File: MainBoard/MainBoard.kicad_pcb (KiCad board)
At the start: 2 copper layers, 50 x 50 mm, 12 parts, among them P0n1 ON, P1 CONN_01X07, P13 CONN_01X07, P14 CONN_01X04, P5 BATTERY, P8 CONN_01X04, U1 4056_CARG

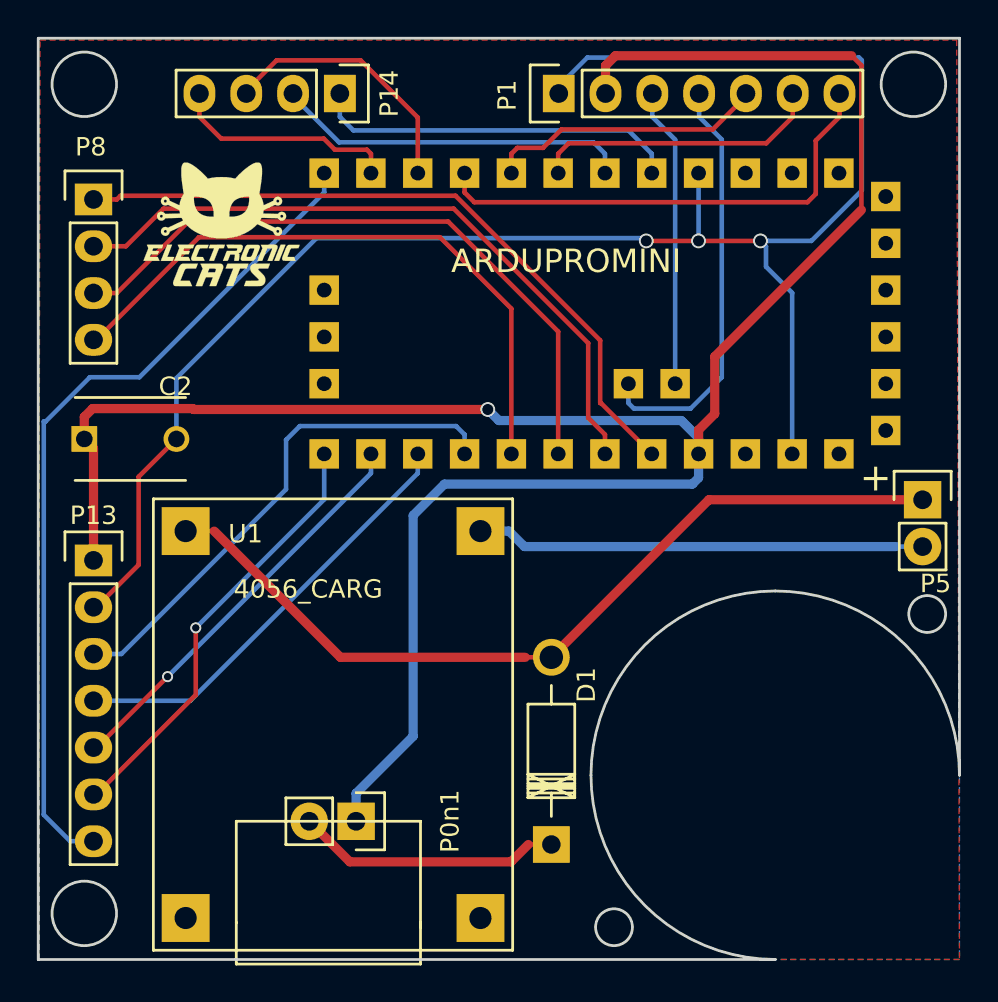
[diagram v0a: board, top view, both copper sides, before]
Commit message: Update referencePCB for schematic MainBoard
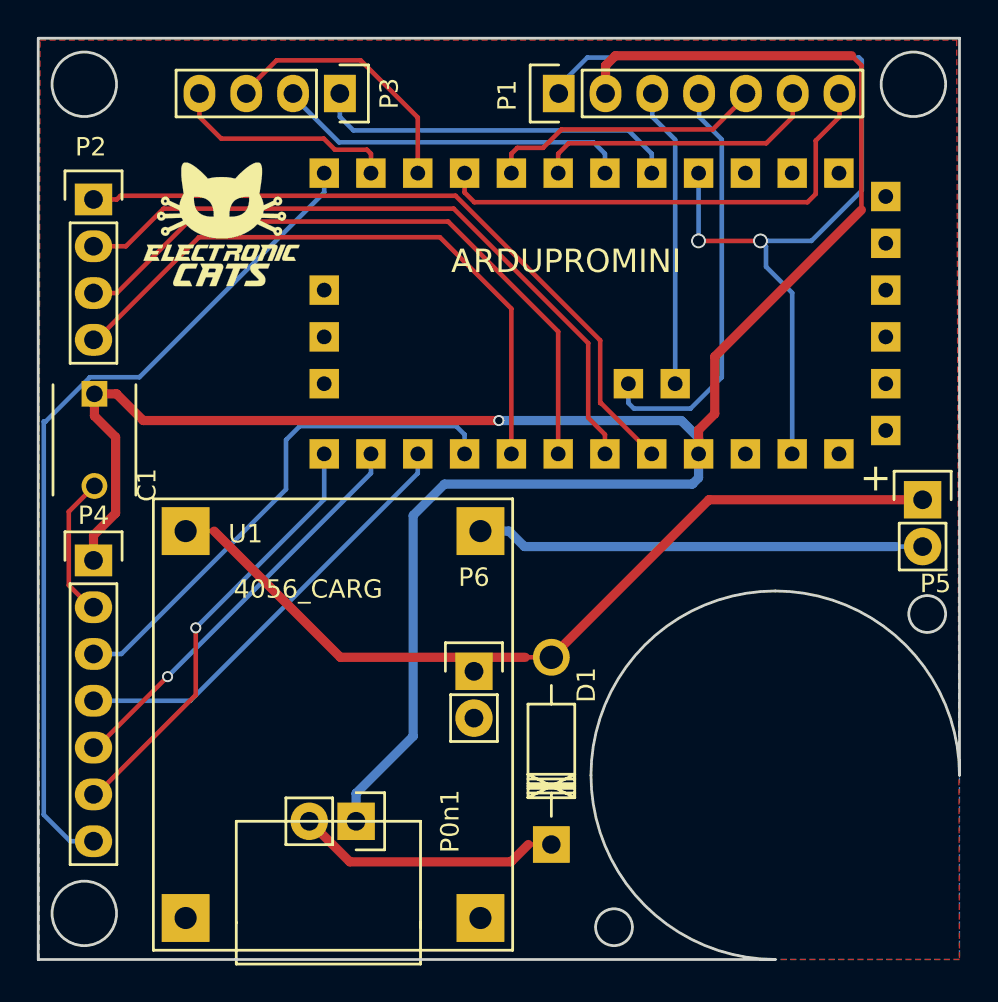
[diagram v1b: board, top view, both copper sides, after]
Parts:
- added P6: BATTERY, Pin_Headers:Pin_Header_Straight_1x02, F.Cu at (108.2, 88.3)
- C1: renamed from C2; value C -> 0.1uF
- P5: value BATTERY -> ON/OFF
- moved C1 2.51 mm to (87.6, 73.2), turned to 270 degrees
- renumbered P8 to P2, P14 to P3, P13 to P4
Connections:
- net A0 renamed /A0
- net A1 renamed /A1
- net A2 renamed /A2
- net A3 renamed /A3
- net D7 renamed /D7
- net D8 renamed /D8
- net DHT/D6 renamed /DHT/D6
- net INT0 renamed /INT0
- net INT1 renamed /INT1
- net MISO renamed /MISO
- net MOSI renamed /MOSI
- net NSS renamed /NSS
- net RST renamed /RST
- net SCK renamed /SCK
- net SCL renamed /SCL
- net SDA renamed /SDA
- net S_RX renamed /S_RX
- net S_TX renamed /S_TX
- P5 pad 1: Net-(D1-Pad2) -> +BATT
- P5 pad 2: Net-(P5-Pad2) -> Net-(D1-Pad1)
- RAW1 pad 1: Net-(RAW1-Pad1) -> (no net)
- RAW1 pad 2: Net-(RAW1-Pad2) -> (no net)
- RAW1 pad 3: Net-(RAW1-Pad3) -> (no net)
- RAW1 pad 4: Net-(RAW1-Pad4) -> (no net)
- RAW1 pad 5: Net-(RAW1-Pad5) -> (no net)
- RAW1 pad 6: Net-(RAW1-Pad6) -> (no net)
- U1 pad 4: Net-(P5-Pad2) -> GND
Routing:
- net Net-(P5-Pad2): track 24.3 -> 0.00 mm
- net GND: track 96.5 -> 81.4 mm, vias 3 -> 2
- net +BATT: track 131.4 -> 144.6 mm
- net Net-(D1-Pad2): track 46.4 -> 34.8 mm
- net Net-(D1-Pad1): track 14.4 -> 15.9 mm

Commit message: Update PCB footprints MainBoard
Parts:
- removed P0n1: ON, Pin_Headers:Pin_Header_Straight_1x02
- moved P5 35.4 mm to (101.8, 96.4), turned to 270 degrees
- moved P6 26.1 mm to (132.6, 79.0)
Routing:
- net GND: track 81.4 -> 93.1 mm
- net +BATT: track 144.6 -> 133.0 mm
- net Net-(D1-Pad2): track 34.8 -> 46.4 mm
- net Net-(D1-Pad1): track 15.9 -> 14.4 mm
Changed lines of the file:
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@@
 (kicad_pcb (version 4) (host pcbnew 4.0.3-stable)
   (general
-    (links 33)
-    (no_connects 3)
+    (links 31)
+    (no_connects 2)
     (area 84.474999 53.824999 134.625001 103.975001)
     (thickness 1.6)
     (drawings 28)
-    (tracks 176)
+    (tracks 183)
     (zones 0)
-    (modules 13)
+    (modules 12)
     (nets 30)
   )
@@
     (add_net /S_RX)
     (add_net /S_TX)
-    (add_net GND)
     (add_net "Net-(D1-Pad1)")
     (add_net "Net-(D1-Pad2)")
@@
     (uvia_drill 0.1)
     (add_net +BATT)
-  )
-  (module Pin_Headers:Pin_Header_Straight_1x02 (layer F.Cu)
-    (at 101.8 96.4 270)
-    (descr "Through hole pin header")
-    (tags "pin header")
-    (fp_text reference P0n1 (at 0 -5.1 270) (layer F.SilkS)
-      (effects (font (size 1 1) (thickness 0.15)))
-    )
-    (fp_text value ON (at 0 -3.1 270) (layer F.Fab)
-      (effects (font (size 1 1) (thickness 0.15)))
-    )
-    (fp_line (start 1.27 1.27) (end 1.27 3.81) (layer F.SilkS) (width 0.15))
-    (fp_line (start 1.55 -1.55) (end 1.55 0) (layer F.SilkS) (width 0.15))
-    (fp_line (start -1.75 -1.75) (end -1.75 4.3) (layer F.CrtYd) (width 0.05))
-    (fp_line (start 1.75 -1.75) (end 1.75 4.3) (layer F.CrtYd) (width 0.05))
-    (fp_line (start -1.75 -1.75) (end 1.75 -1.75) (layer F.CrtYd) (width 0.05))
-    (fp_line (start -1.75 4.3) (end 1.75 4.3) (layer F.CrtYd) (width 0.05))
-    (fp_line (start 1.27 1.27) (end -1.27 1.27) (layer F.SilkS) (width 0.15))
-    (fp_line (start -1.55 0) (end -1.55 -1.55) (layer F.SilkS) (width 0.15))
-    (fp_line (start -1.55 -1.55) (end 1.55 -1.55) (layer F.SilkS) (width 0.15))
-    (fp_line (start -1.27 1.27) (end -1.27 3.81) (layer F.SilkS) (width 0.15))
-    (fp_line (start -1.27 3.81) (end 1.27 3.81) (layer F.SilkS) (width 0.15))
-    (pad 1 thru_hole rect (at 0 0 270) (size 2.032 2.032) (drill 1.016) (layers *.Cu *.Mask F.SilkS)
-      (net 3 +BATT))
-    (pad 2 thru_hole oval (at 0 2.54 270) (size 2.032 2.032) (drill 1.016) (layers *.Cu *.Mask F.SilkS)
-      (net 11 "Net-(D1-Pad1)"))
-    (model Pin_Headers.3dshapes/Pin_Header_Straight_1x02.wrl
-      (at (xyz 0 -0.05 0))
-      (scale (xyz 1 1 1))
-      (rotate (xyz 0 0 90))
-    )
+    (add_net GND)
   )
   (module 4056_lipoCharg (layer F.Cu)
@@
   )
   (module Pin_Headers:Pin_Header_Straight_1x02 (layer F.Cu)
-    (at 132.55 78.95)
+    (at 101.79 96.4 270)
     (descr "Through hole pin header")
     (tags "pin header")
-    (fp_text reference P5 (at 0.7 4.55) (layer F.SilkS)
-      (effects (font (size 1 1) (thickness 0.15)))
-    )
-    (fp_text value ON/OFF (at -1.95 3.05 90) (layer F.Fab)
+    (fp_text reference P5 (at 0.7 4.55 270) (layer F.SilkS)
+      (effects (font (size 1 1) (thickness 0.15)))
+    )
+    (fp_text value ON/OFF (at -1.95 3.05 360) (layer F.Fab)
       (effects (font (size 1 1) (thickness 0.15)))
     )
@@
     (fp_line (start -1.27 1.27) (end -1.27 3.81) (layer F.SilkS) (width 0.15))
     (fp_line (start -1.27 3.81) (end 1.27 3.81) (layer F.SilkS) (width 0.15))
-    (pad 1 thru_hole rect (at 0 0) (size 2.032 2.032) (drill 1.016) (layers *.Cu *.Mask F.SilkS)
+    (pad 1 thru_hole rect (at 0 0 270) (size 2.032 2.032) (drill 1.016) (layers *.Cu *.Mask F.SilkS)
       (net 3 +BATT))
-    (pad 2 thru_hole oval (at 0 2.54) (size 2.032 2.032) (drill 1.016) (layers *.Cu *.Mask F.SilkS)
+    (pad 2 thru_hole oval (at 0 2.54 270) (size 2.032 2.032) (drill 1.016) (layers *.Cu *.Mask F.SilkS)
       (net 11 "Net-(D1-Pad1)"))
     (model Pin_Headers.3dshapes/Pin_Header_Straight_1x02.wrl
@@
   )
   (module Pin_Headers:Pin_Header_Straight_1x02 (layer F.Cu)
-    (at 108.2 88.26)
+    (at 132.575 78.96)
     (descr "Through hole pin header")
     (tags "pin header")
-    (fp_text reference P6 (at 0 -5.1) (layer F.SilkS)
-      (effects (font (size 1 1) (thickness 0.15)))
-    )
-    (fp_text value BATTERY (at 0 -3.1) (layer F.Fab)
+    (fp_text reference P6 (at 0.75 -2.56) (layer F.SilkS)
+      (effects (font (size 1 1) (thickness 0.15)))
+    )
+    (fp_text value BATTERY (at -2.475 2.99 90) (layer F.Fab)
       (effects (font (size 1 1) (thickness 0.15)))
     )
@@
   (gr_line (start 84.55 103.9) (end 84.55 53.9) (layer Edge.Cuts) (width 0.15))
   (gr_line (start 84.55 53.9) (end 134.55 53.9) (layer Edge.Cuts) (width 0.15))
+  (segment (start 120.386543 64.9) (end 123.75 64.9) (width 0.5) (layer F.Cu) (net 1))
+  (segment (start 120.39 61.22) (end 120.39 64.896543) (width 0.5) (layer B.Cu) (net 1))
+  (segment (start 120.39 64.896543) (end 120.386543 64.9) (width 0.5) (layer B.Cu) (net 1))
+  (segment (start 110.94 81.49) (end 128.275 81.49) (width 0.5) (layer B.Cu) (net 1))
+  (segment (start 125.47 77.76) (end 128.275 80.565) (width 0.5) (layer B.Cu) (net 1))
+  (segment (start 128.275 81.49) (end 128.5 81.49) (width 0.5) (layer B.Cu) (net 1))
+  (segment (start 125.47 76.46) (end 125.47 77.76) (width 0.5) (layer B.Cu) (net 1))
+  (segment (start 128.275 80.565) (end 128.275 81.49) (width 0.5) (layer B.Cu) (net 1))
+  (segment (start 125.47 76.46) (end 125.47 67.95) (width 0.5) (layer B.Cu) (net 1))
+  (segment (start 123.75 64.9) (end 123.75 66.23) (width 0.5) (layer B.Cu) (net 1))
+  (segment (start 123.75 66.23) (end 125.47 67.95) (width 0.5) (layer B.Cu) (net 1))
+  (segment (start 131.13816 81.5) (end 131.12816 81.49) (width 0.25) (layer B.Cu) (net 1))
+  (segment (start 128.5 81.49) (end 131.11316 81.49) (width 0.5) (layer B.Cu) (net 1))
+  (segment (start 132.575 81.5) (end 131.13816 81.5) (width 0.25) (layer B.Cu) (net 1))
+  (segment (start 131.12816 81.49) (end 128.5 81.49) (width 0.25) (layer B.Cu) (net 1))
   (segment (start 87.6 78.2) (end 86.208999 79.591001) (width 0.25) (layer F.Cu) (net 1))
   (segment (start 86.208999 79.591001) (end 86.208999 83.591399) (width 0.25) (layer F.Cu) (net 1))
@@
   (segment (start 87.3976 84.78) (end 87.55 84.78) (width 0.25) (layer F.Cu) (net 1))
   (via (at 120.386543 64.9) (size 0.8) (drill 0.6) (layers F.Cu B.Cu) (net 1))
-  (segment (start 120.39 64.896543) (end 120.386543 64.9) (width 0.25) (layer B.Cu) (net 1))
-  (segment (start 120.39 61.22) (end 120.39 64.896543) (width 0.25) (layer B.Cu) (net 1))
-  (segment (start 120.386543 64.9) (end 123.75 64.9) (width 0.25) (layer F.Cu) (net 1))
   (via (at 123.75 64.9) (size 0.8) (drill 0.6) (layers F.Cu B.Cu) (net 1))
-  (segment (start 123.75 64.9) (end 124.049999 65.199999) (width 0.25) (layer B.Cu) (net 1))
   (segment (start 124.174264 64.9) (end 123.75 64.9) (width 0.25) (layer B.Cu) (net 1))
   (segment (start 129.25 55.1) (end 129.25 62.165002) (width 0.25) (layer B.Cu) (net 1))
@@
   (segment (start 126.515002 64.9) (end 124.174264 64.9) (width 0.25) (layer B.Cu) (net 1))
   (segment (start 129.25 62.165002) (end 126.515002 64.9) (width 0.25) (layer B.Cu) (net 1))
-  (segment (start 124.049999 65.199999) (end 124.049999 66.299999) (width 0.25) (layer B.Cu) (net 1))
-  (segment (start 125.47 67.72) (end 125.47 76.46) (width 0.25) (layer B.Cu) (net 1))
-  (segment (start 124.049999 66.299999) (end 125.47 67.72) (width 0.25) (layer B.Cu) (net 1))
   (segment (start 112.8 56.9) (end 112.8 56.5) (width 0.25) (layer B.Cu) (net 1))
   (segment (start 87.55 84.78) (end 87.7024 84.78) (width 0.25) (layer F.Cu) (net 1))
   (segment (start 108.55 80.65) (end 110.1 80.65) (width 0.5) (layer B.Cu) (net 1))
   (segment (start 110.1 80.65) (end 110.94 81.49) (width 0.5) (layer B.Cu) (net 1))
-  (segment (start 110.94 81.49) (end 131.11316 81.49) (width 0.5) (layer B.Cu) (net 1))
+  (segment (start 131.11316 81.49) (end 132.55 81.49) (width 0.25) (layer B.Cu) (net 1))
   (segment (start 92.55 80.65) (end 94.1 80.65) (width 0.25) (layer F.Cu) (net 2))
   (segment (start 94.1 80.65) (end 100.95 87.5) (width 0.5) (layer F.Cu) (net 2))
@@
   (segment (start 100.95 87.5) (end 110.986508 87.5) (width 0.5) (layer F.Cu) (net 2))
   (segment (start 120.95 78.95) (end 112.4 87.5) (width 0.5) (layer F.Cu) (net 2))
+  (segment (start 132.55 78.95) (end 120.95 78.95) (width 0.5) (layer F.Cu) (net 2))
   (segment (start 87.55 82.24) (end 87.55 80.8764) (width 0.5) (layer F.Cu) (net 3))
   (segment (start 87.55 80.8764) (end 88.750001 79.676399) (width 0.5) (layer F.Cu) (net 3))
@@
   (segment (start 90.25 74.65) (end 109.55 74.65) (width 0.5) (layer F.Cu) (net 3))
   (via (at 109.55 74.65) (size 0.6) (drill 0.4) (layers F.Cu B.Cu) (net 3))
-  (segment (start 132.55 78.95) (end 120.95 78.95) (width 0.5) (layer F.Cu) (net 3))
   (segment (start 104.9 79.8) (end 106.6 78.1) (width 0.5) (layer B.Cu) (net 3))
   (segment (start 120.09546 78.05454) (end 120.39 77.76) (width 0.5) (layer B.Cu) (net 3))
@@
   (segment (start 129.22861 55.37861) (end 129.22861 63.22139) (width 0.25) (layer F.Cu) (net 3))
   (segment (start 128.7 54.85) (end 129.22861 55.37861) (width 0.25) (layer F.Cu) (net 3))
-  (segment (start 131.11316 81.49) (end 132.55 81.49) (width 0.25) (layer B.Cu) (net 11))
   (segment (start 101.46 98.6) (end 110.21051 98.6) (width 0.5) (layer F.Cu) (net 11))
   (segment (start 110.21051 98.6) (end 111.15051 97.66) (width 0.5) (layer F.Cu) (net 11))

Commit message: Correction pad, via and logo
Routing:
- net GND: track 93.1 -> 89.8 mm
- net /RST: track 46.1 -> 44.4 mm
- net Net-(D1-Pad1): track 14.4 -> 15.3 mm
- net Net-(D1-Pad2): track 46.4 -> 47.1 mm
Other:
- board text added: "CaTSat 1.1v"

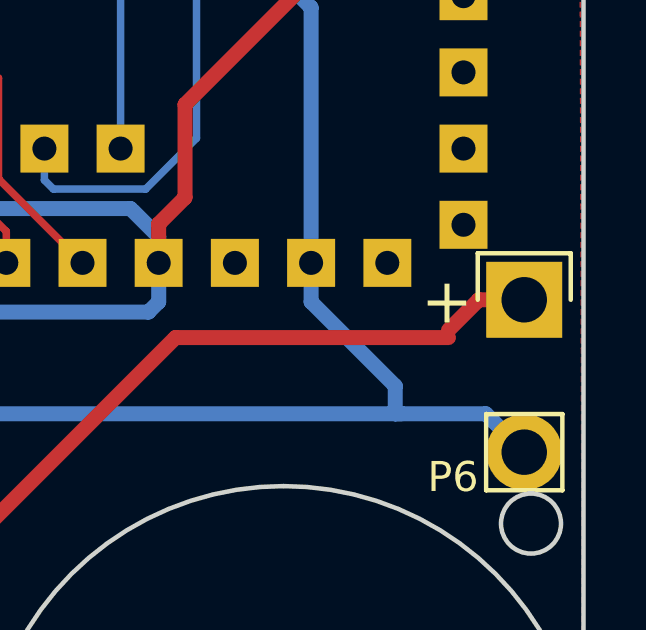
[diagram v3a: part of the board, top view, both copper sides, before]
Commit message: Added label Main Board
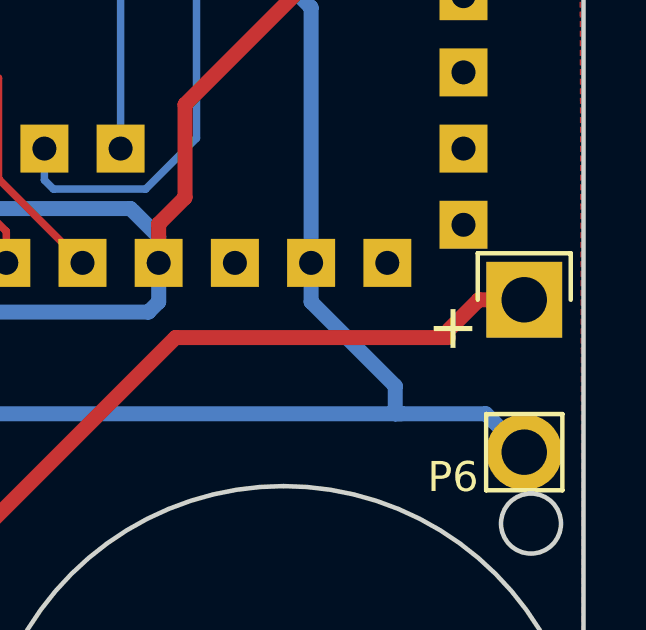
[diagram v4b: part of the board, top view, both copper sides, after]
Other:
- board text added: "+BATT GND"
- board text added: "A3 A2 A1 A0"
- board text added: "D6 D7"
- board text added: "D6/DHT"
- board text added: "GND +BATT"
- board text added: "INT1 INT0"
- board text added: "MOSI NSS"
- board text added: "RST"
- board text added: "SCK MISO"
- board text added: "SCL SDA"
- board text added: "S_RX S_TX"
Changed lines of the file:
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@@
     (area 84.474999 53.824999 134.625001 103.975001)
     (thickness 1.6)
-    (drawings 29)
+    (drawings 40)
     (tracks 183)
     (zones 0)
@@
   )
   (layers
-    (0 F.Cu signal hide)
-    (31 B.Cu signal hide)
+    (0 F.Cu signal)
+    (31 B.Cu signal)
     (32 B.Adhes user)
     (33 F.Adhes user)
@@
       (effects (font (size 1 1) (thickness 0.15)))
     )
-    (fp_text value BATTERY (at -2.575 1.44 90) (layer B.SilkS)
-      (effects (font (size 1 1) (thickness 0.15)) (justify mirror))
+    (fp_text value BATTERY (at -2.575 2.24 90) (layer B.SilkS)
+      (effects (font (size 1.2 1.2) (thickness 0.3)) (justify mirror))
     )
     (fp_line (start 1.27 2.54) (end 1.27 5.08) (layer F.SilkS) (width 0.15))
@@
     (fp_line (start -1.99898 -23.50008) (end -1.09982 -21.20138) (layer B.SilkS) (width 0.15))
   )
-  (gr_text "CaTSat 1.1v" (at 115.2 66) (layer B.SilkS)
+  (gr_text D6/DHT (at 128.2 61.6 90) (layer B.SilkS)
+    (effects (font (size 1.2 1.2) (thickness 0.3)) (justify mirror))
+  )
+  (gr_text "S_RX\nS_TX" (at 124 60.6 90) (layer B.SilkS)
+    (effects (font (size 1.2 1.2) (thickness 0.3)) (justify mirror))
+  )
+  (gr_text "SCL\nSDA" (at 119 60 90) (layer B.SilkS)
+    (effects (font (size 1.2 1.2) (thickness 0.3)) (justify mirror))
+  )
+  (gr_text "GND\n+BATT" (at 114 61 90) (layer B.SilkS)
+    (effects (font (size 1.2 1.2) (thickness 0.3)) (justify mirror))
+  )
+  (gr_text "INT1\nINT0" (at 99.6 60.4 90) (layer B.SilkS)
+    (effects (font (size 1.2 1.2) (thickness 0.3)) (justify mirror))
+  )
+  (gr_text "D6\nD7" (at 94.6 59.6 90) (layer B.SilkS)
+    (effects (font (size 1.2 1.2) (thickness 0.3)) (justify mirror))
+  )
+  (gr_text RST (at 91.2 97.8) (layer B.SilkS)
+    (effects (font (size 1.2 1.2) (thickness 0.3)) (justify mirror))
+  )
+  (gr_text "MOSI\nNSS" (at 91.4 93.6) (layer B.SilkS)
+    (effects (font (size 1.2 1.2) (thickness 0.3)) (justify mirror))
+  )
+  (gr_text "SCK\nMISO" (at 91.4 88.6) (layer B.SilkS)
+    (effects (font (size 1.2 1.2) (thickness 0.3)) (justify mirror))
+  )
+  (gr_text "+BATT\nGND" (at 91.6 84) (layer B.SilkS)
+    (effects (font (size 1.2 1.2) (thickness 0.3)) (justify mirror))
+  )
+  (gr_text "A3\nA2\nA1\nA0" (at 91.4 66.6) (layer B.SilkS)
     (effects (font (size 1.5 1.5) (thickness 0.3)) (justify mirror))
   )
-  (gr_text " Main \nBoard" (at 94.2 62.4) (layer B.SilkS)
+  (gr_text "CaTSat 1.1v" (at 108.2 70.2) (layer B.SilkS)
     (effects (font (size 1.5 1.5) (thickness 0.3)) (justify mirror))
   )
-  (gr_text "+\n" (at 130 77.75) (layer F.SilkS)
+  (gr_text " Main \nBoard" (at 107.4 66.4) (layer B.SilkS)
+    (effects (font (size 1.5 1.5) (thickness 0.3)) (justify mirror))
+  )
+  (gr_text "+\n" (at 130.2 78.6) (layer F.SilkS)
     (effects (font (size 1.5 1.5) (thickness 0.3)))
   )
